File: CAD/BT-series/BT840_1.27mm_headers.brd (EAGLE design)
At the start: 33.4 x 25.1 mm, 64 parts, among them J1 SM02B-SRSS-TB(LF)(SN), U1 TPD4S012DRYR, U2 BT840, U3 LP5907MFX-3.3/NOPB, U4 LP5907MFX-3.3/NOPB, U5 ADS131M08IPBS, U6 BQ24072RGTR, U7 DX4R005JJ2R1800, X1 ABM3B-8.000MHZ-B2-T, X2 FC-12M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

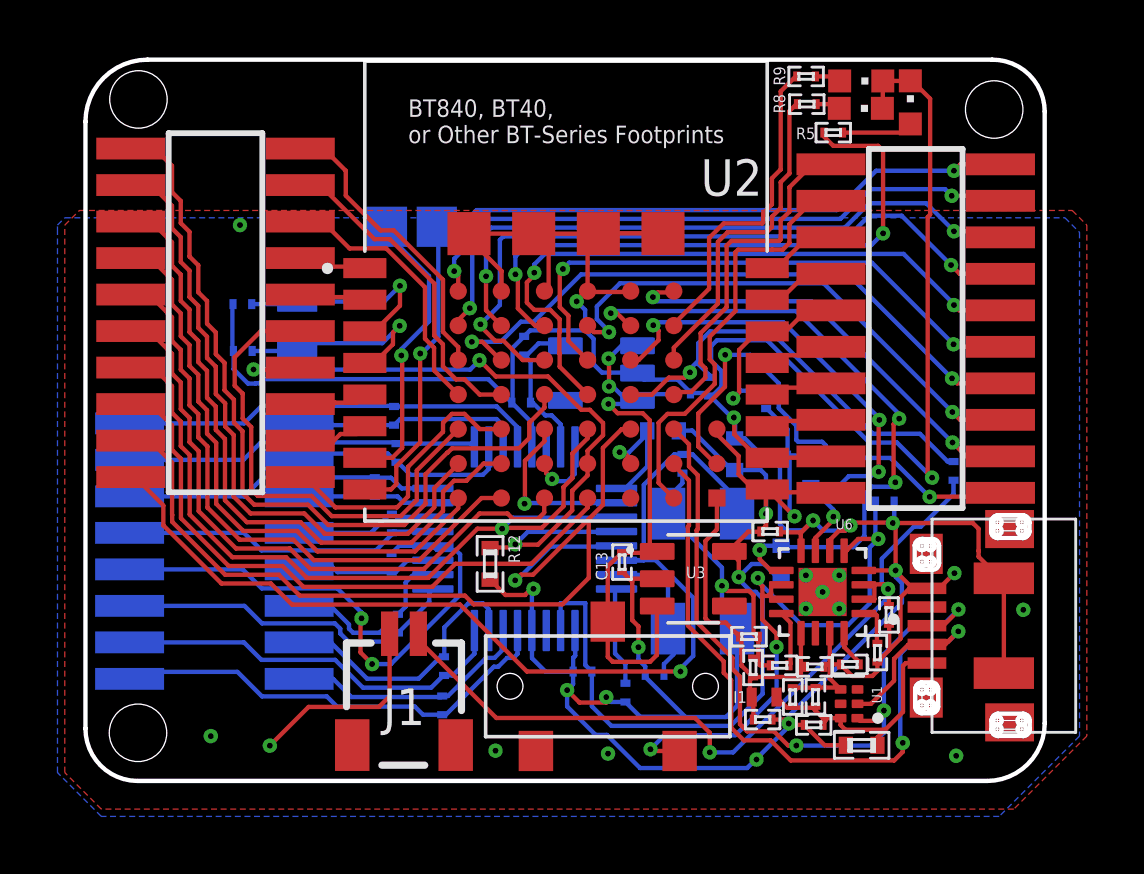
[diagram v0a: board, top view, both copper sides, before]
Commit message: modifed io order on bt840, some nrf52840 firmware cleanup (need to update with compass and audio too)
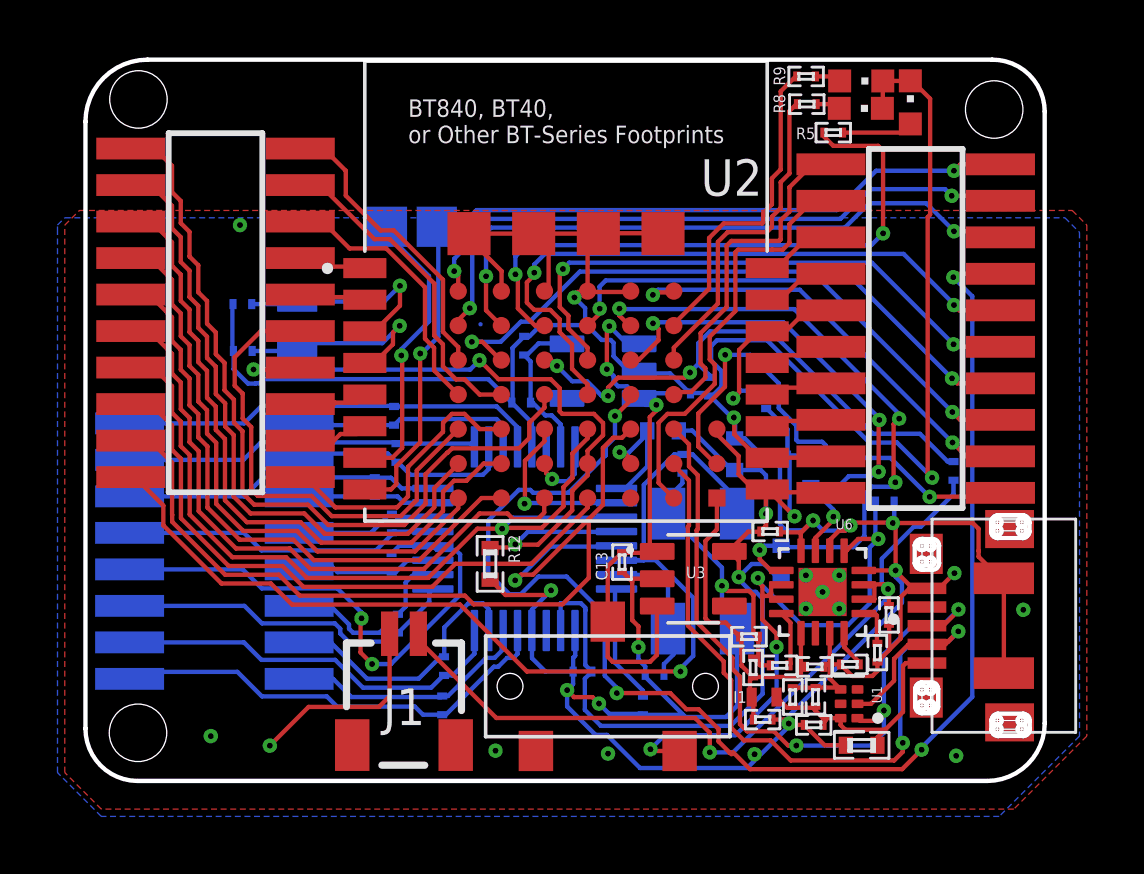
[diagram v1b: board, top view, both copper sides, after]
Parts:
- moved C6 0.76 mm to (26.7, 44.5)
- moved U4 0.09 mm to (25.3, 56.1)
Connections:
- removed net P30_AIN6: U2.B2, X4.8
- new net P16: U2.D3, X4.8
- net CUR_DETECT: now also U2.B2; no longer U2.D3
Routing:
- net P16: track 0.00 -> 48.9 mm, vias 0 -> 4
- net P30_AIN6: track 24.6 -> 0.00 mm, vias 2 -> 0
- net CUR_DETECT: track 15.3 -> 18.8 mm, vias 1 -> 3
- net CAP: track 3.45 -> 4.15 mm
- net P24: track 18.3 -> 17.6 mm

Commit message: fixed cur_detect compatibility for bt40/bt840
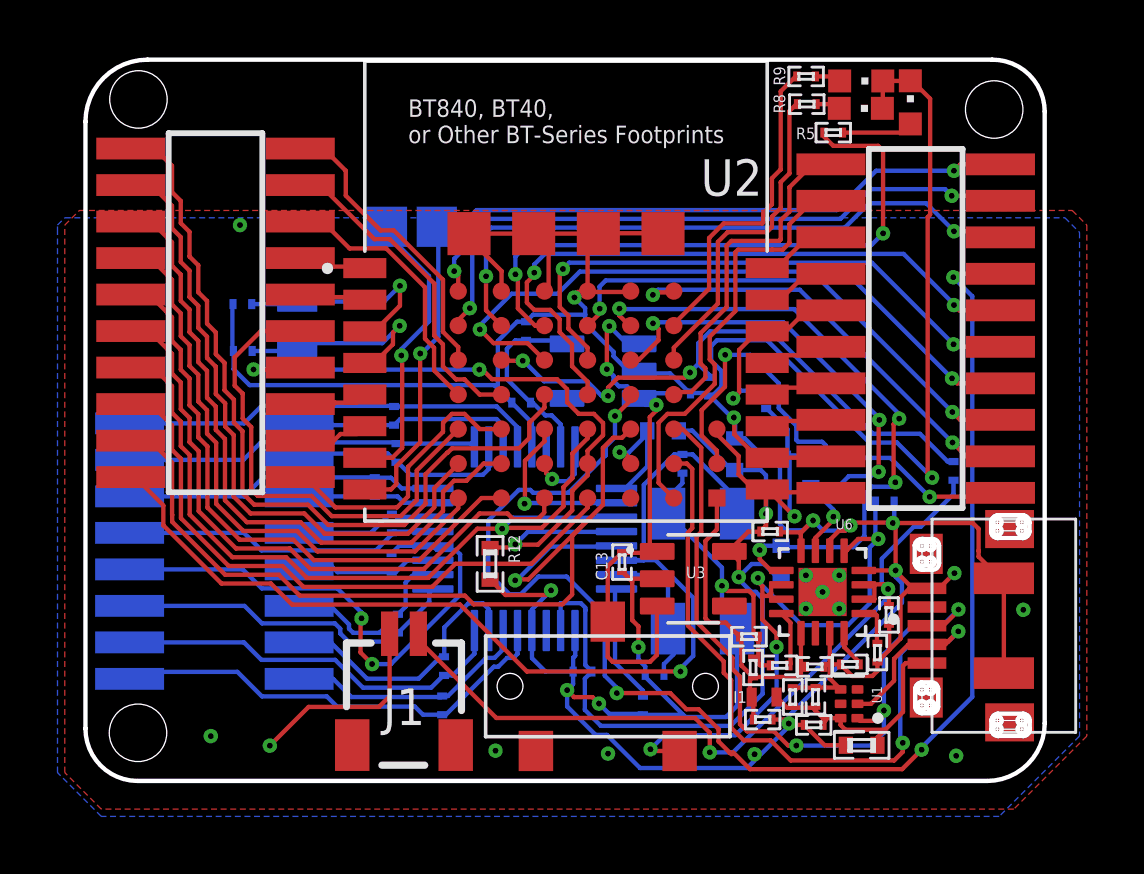
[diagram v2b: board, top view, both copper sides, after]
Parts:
- moved C8 0.51 mm to (22.7, 57.5)
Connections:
- removed net P29_AIN5: U2.A2, X4.14
- new net P30_AIN6: U2.B2, X4.14
- net CUR_DETECT: now also U2.A2; no longer U2.B2
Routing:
- net P30_AIN6: track 0.00 -> 23.3 mm, vias 0 -> 2
- net P29_AIN5: track 22.3 -> 0.00 mm, vias 2 -> 0
- net CUR_DETECT: track 18.8 -> 20.5 mm
- net AVDD: track 5.56 -> 6.62 mm
- net GND: track 178.6 -> 179.2 mm

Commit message: broke out the last gpio
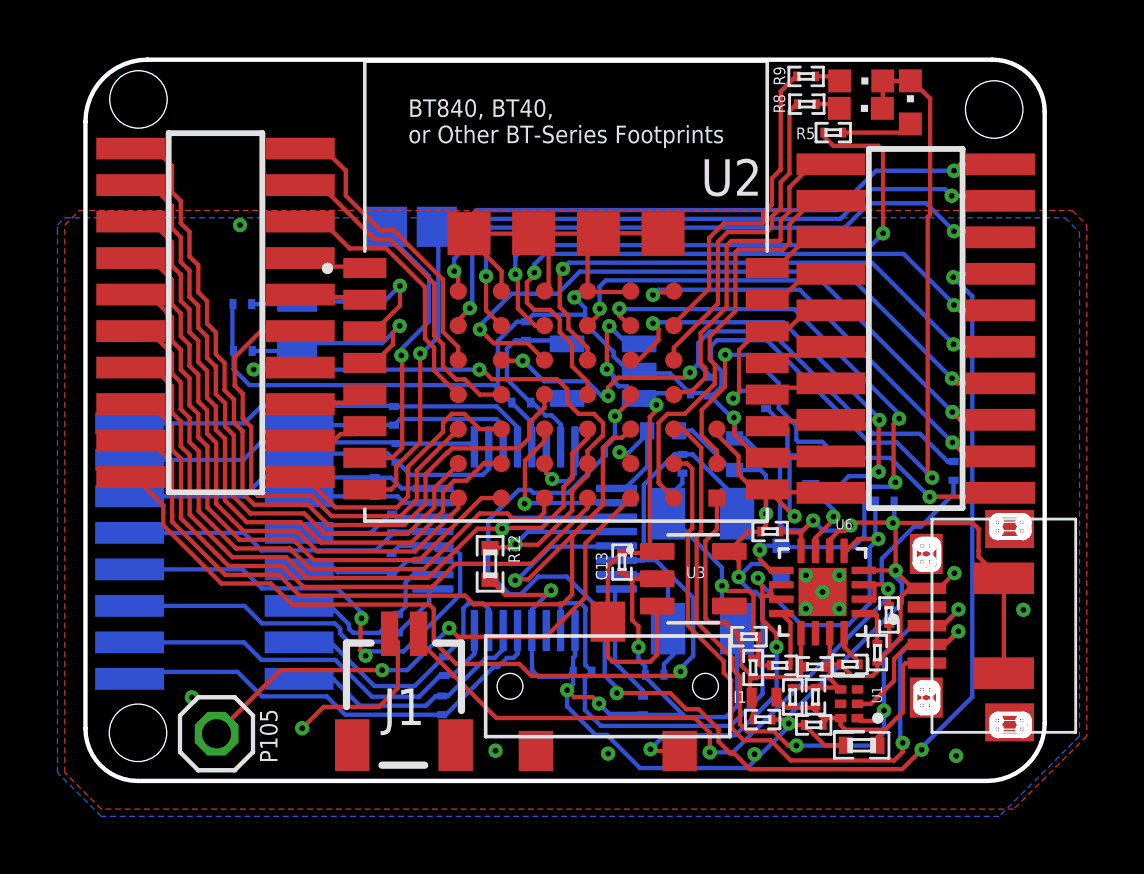
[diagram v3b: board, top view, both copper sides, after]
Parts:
- added JP1: (no value), pinhead:1X01
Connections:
- net P105: now also JP1.1
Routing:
- net P105: track 0.06 -> 19.2 mm, vias 0 -> 2
- net CLKOUT: track 37.3 -> 38.0 mm
- net GND: track 179.2 -> 178.5 mm
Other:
- board text added: "P105"

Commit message: Update BT840_1.27mm_headers.brd
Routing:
- net GND: track 178.5 -> 178.7 mm, vias 22 -> 24
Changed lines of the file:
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@@
 <wire x1="22.85946875" y1="46.918859375" x2="22.856" y2="46.922328125" width="0.1524" layer="16"/>
 <wire x1="22.856" y1="47.106653125" x2="22.856" y2="46.922328125" width="0.1524" layer="16"/>
-<wire x1="22.85946875" y1="46.918859375" x2="22.85946875" y2="45.7313125" width="0.1524" layer="16"/>
+<wire x1="22.85946875" y1="46.918859375" x2="22.85946875" y2="46.10379375" width="0.1524" layer="16"/>
+<wire x1="22.85946875" y1="46.10379375" x2="22.85946875" y2="45.7313125" width="0.1524" layer="16"/>
 <wire x1="24.28998125" y1="45.674884375" x2="24.28998125" y2="45.2405875" width="0.1524" layer="16"/>
 <wire x1="24.08199375" y1="45.0326" x2="24.28998125" y2="45.2405875" width="0.1524" layer="16"/>
@@
 <wire x1="37.02848125" y1="48.574990625" x2="37.55753125" y2="49.104040625" width="0.1524" layer="1"/>
 <via x="37.55753125" y="49.104040625" extent="1-16" drill="0.2"/>
-<wire x1="17.90535" y1="46.99624375" x2="18.192875" y2="46.70871875" width="0.1524" layer="1"/>
-<wire x1="18.192875" y1="46.70871875" x2="18.192875" y2="45.1075" width="0.1524" layer="1"/>
+<wire x1="18.192875" y1="46.198434375" x2="17.90535" y2="46.485959375" width="0.1524" layer="1"/>
+<wire x1="17.90535" y1="46.99624375" x2="17.90535" y2="46.485959375" width="0.1524" layer="1"/>
+<wire x1="18.192875" y1="46.198434375" x2="18.192875" y2="45.1075" width="0.1524" layer="1"/>
 <wire x1="18.192875" y1="45.1075" x2="17.534865625" y2="44.449490625" width="0.1524" layer="1"/>
 <wire x1="35.06489375" y1="66.228975" x2="35.06489375" y2="65.2904" width="0.1524" layer="1"/>
@@
 <wire x1="25.698209375" y1="56.650634375" x2="25.698209375" y2="56.80199375" width="0.1524" layer="16"/>
 <wire x1="25.698209375" y1="56.80199375" x2="24.7093875" y2="57.790815625" width="0.1524" layer="16"/>
-<wire x1="39.27666875" y1="48.924990625" x2="39.9542" y2="47.8282" width="0" layer="19" extent="1-1"/>
-<wire x1="24.793384375" y1="58.916821875" x2="24.3358" y2="58.694828125" width="0" layer="19" extent="1-1"/>
-<wire x1="30.60395" y1="42.8030625" x2="31.210890625" y2="44.0093125" width="0" layer="19" extent="1-1"/>
-<wire x1="25.505665625" y1="42.824653125" x2="26.6870125" y2="44.2095875" width="0" layer="19" extent="16-16"/>
-<wire x1="12.7" y1="61.214" x2="12.458565625" y2="58.46470625" width="0" layer="19" extent="16-16"/>
-<wire x1="21.59" y1="42.926" x2="24.08199375" y2="45.0326" width="0" layer="19" extent="1-1"/>
-<wire x1="37.6174" y1="42.7482" x2="39.27666875" y2="45.624990625" width="0" layer="19" extent="1-1"/>
-<wire x1="18.192875" y1="46.70871875" x2="21.401534375" y2="48.8761125" width="0" layer="19" extent="1-1"/>
-<wire x1="11.026903125" y1="44.783246875" x2="14.86484375" y2="43.7078125" width="0" layer="19" extent="1-1"/>
+<wire x1="22.85946875" y1="46.10379375" x2="22.955425" y2="46.10379375" width="0.1524" layer="16"/>
+<wire x1="22.955425" y1="46.10379375" x2="23.04795625" y2="46.0112625" width="0.1524" layer="16"/>
+<via x="23.04795625" y="46.0112625" extent="1-16" drill="0.2"/>
+<via x="18.278346875" y="43.20184375" extent="1-16" drill="0.2"/>
 </signal>
 <signal name="AVDD">
@@
 <wire x1="26.293384375" y1="54.116821875" x2="25.990959375" y2="53.814396875" width="0.1524" layer="1"/>
 <wire x1="25.68116875" y1="53.814396875" x2="25.990959375" y2="53.814396875" width="0.1524" layer="1"/>
-<wire x1="24.25711875" y1="50.4079625" x2="24.83420625" y2="50.98505" width="0.1524" layer="1"/>
+<wire x1="24.006165625" y1="50.157009375" x2="24.83420625" y2="50.98505" width="0.1524" layer="1"/>
 <wire x1="24.83420625" y1="50.98505" x2="25.325496875" y2="51.476340625" width="0.1524" layer="1"/>
 <wire x1="25.325496875" y1="51.476340625" x2="25.325496875" y2="53.458725" width="0.1524" layer="1"/>
@@
 <wire x1="20.526246875" y1="48.3209625" x2="20.829015625" y2="48.01819375" width="0.1524" layer="1"/>
 <wire x1="24.83420625" y1="50.98505" x2="24.83420625" y2="50.98809375" width="0.1524" layer="1"/>
-<wire x1="24.25711875" y1="48.359178125" x2="24.25711875" y2="50.4079625" width="0.1524" layer="1"/>
-<wire x1="20.829015625" y1="48.01819375" x2="23.916134375" y2="48.01819375" width="0.1524" layer="1"/>
-<wire x1="23.916134375" y1="48.01819375" x2="24.25711875" y2="48.359178125" width="0.1524" layer="1"/>
+<wire x1="24.006165625" y1="48.2916125" x2="24.006165625" y2="50.157009375" width="0.1524" layer="1"/>
+<wire x1="20.829015625" y1="48.01819375" x2="23.732746875" y2="48.01819375" width="0.1524" layer="1"/>
+<wire x1="23.732746875" y1="48.01819375" x2="24.006165625" y2="48.2916125" width="0.1524" layer="1"/>
 <wire x1="22.272503125" y1="48.85240625" x2="22.30719375" y2="48.887096875" width="0.1524" layer="1"/>
 <wire x1="22.30719375" y1="48.887096875" x2="22.733209375" y2="48.887096875" width="0.1524" layer="1"/>
@@
 <contactref element="U2" pad="D6"/>
 <wire x1="26.233003125" y1="51.716821875" x2="26.293384375" y2="51.716821875" width="0.1524" layer="1"/>
-<wire x1="26.293384375" y1="51.716821875" x2="24.716740625" y2="50.140178125" width="0.1524" layer="1"/>
-<wire x1="24.716740625" y1="48.260803125" x2="23.346115625" y2="46.890178125" width="0.1524" layer="1"/>
-<wire x1="24.716740625" y1="50.140178125" x2="24.716740625" y2="48.260803125" width="0.1524" layer="1"/>
-<wire x1="20.28250625" y1="46.890178125" x2="19.979321875" y2="47.1933625" width="0.1524" layer="1"/>
+<wire x1="26.293384375" y1="51.716821875" x2="26.008396875" y2="51.716821875" width="0.1524" layer="1"/>
+<wire x1="26.008396875" y1="51.716821875" x2="24.3164375" y2="50.0248625" width="0.1524" layer="1"/>
+<wire x1="24.3164375" y1="48.14574375" x2="23.872403125" y2="47.701709375" width="0.1524" layer="1"/>
+<wire x1="24.3164375" y1="50.0248625" x2="24.3164375" y2="48.14574375" width="0.1524" layer="1"/>
 <via x="19.979321875" y="47.1933625" extent="1-16" drill="0.2"/>
-<wire x1="23.346115625" y1="46.890178125" x2="20.28250625" y2="46.890178125" width="0.1524" layer="1"/>
+<wire x1="19.979321875" y1="47.1933625" x2="20.48766875" y2="47.701709375" width="0.1524" layer="1"/>
+<wire x1="23.872403125" y1="47.701709375" x2="20.48766875" y2="47.701709375" width="0.1524" layer="1"/>
 <wire x1="19.979321875" y1="47.1933625" x2="18.51535625" y2="45.729396875" width="0.1524" layer="16"/>
 <wire x1="18.51535625" y1="45.729396875" x2="17.645125" y2="45.729396875" width="0.1524" layer="16"/>

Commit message: update
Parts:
- moved JP1 0.76 mm to (12.5, 43.1)
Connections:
- removed net CLKIN: C3.1, U5.23, X1.1
- new net 8.192MHZ: C3.1, U5.23, X1.1, X3.19
- net CLKOUT: no longer X3.19
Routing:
- net 8.192MHZ: track 0.00 -> 30.6 mm, vias 0 -> 1
- net CLKOUT: track 38.0 -> 8.41 mm, vias 1 -> 0
- net CLKIN: track 5.29 -> 0.00 mm
